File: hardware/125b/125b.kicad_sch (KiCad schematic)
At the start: 52 parts, among them J1 Guitar in, J10 Barrel_Jack, J11 NRJ6HF, J2 TC2050, J3 Conn_02x05_Odd_Even_MountingP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, SW1 Switch 1, SW2 Switch 2, SW3 RotaryEncoder_Switch, SW4 SW_DIP_x02, U1 TL074, U2 L78L05_TO92

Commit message: Start work on SMD caps and resistors
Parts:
- removed J2: TC2050, Connector_IDC:IDC-Header_2x05_P2.54mm_Vertical, symbol Connector:TC2050
- C10: renamed from C7; footprint Capacitor_THT:C_Rect_L7.0mm_W2.5mm_P5.00mm -> Capacitor_SMD:C_0805_2012Metric
- C11: renamed from C9; footprint Capacitor_THT:C_Rect_L7.0mm_W2.5mm_P5.00mm -> Capacitor_SMD:C_0805_2012Metric
- C12: renamed from C10; footprint Capacitor_THT:C_Rect_L7.0mm_W2.5mm_P5.00mm -> Capacitor_SMD:C_0805_2012Metric
- C2: renamed from C3; footprint Capacitor_THT:C_Rect_L7.0mm_W2.5mm_P5.00mm -> Capacitor_SMD:C_0805_2012Metric
- C3: renamed from C2; footprint Capacitor_THT:C_Rect_L7.0mm_W2.5mm_P5.00mm -> Capacitor_SMD:C_0805_2012Metric
- C4, C5, C6, C8: footprint Capacitor_THT:C_Rect_L7.0mm_W2.5mm_P5.00mm -> Capacitor_SMD:C_0805_2012Metric
- C7: renamed from C11; footprint Capacitor_THT:C_Rect_L7.0mm_W2.5mm_P5.00mm -> Capacitor_SMD:C_0805_2012Metric
- C9: renamed from C12; footprint Capacitor_THT:C_Rect_L7.0mm_W2.5mm_P5.00mm -> Capacitor_SMD:C_0805_2012Metric
- J3: footprint (none) -> Connector_IDC:IDC-Header_2x05_P2.54mm_Vertical
- R1: footprint Resistor_THT:R_Axial_DIN0207_L6.3mm_D2.5mm_P10.16mm_Horizontal -> Resistor_SMD:R_1206_3216Metric
- R10: renamed from R8; footprint Resistor_THT:R_Axial_DIN0207_L6.3mm_D2.5mm_P10.16mm_Horizontal -> Resistor_SMD:R_0805_2012Metric
- R11: renamed from R9; footprint Resistor_THT:R_Axial_DIN0207_L6.3mm_D2.5mm_P10.16mm_Horizontal -> Resistor_SMD:R_0805_2012Metric
- R12: renamed from R10; footprint Resistor_THT:R_Axial_DIN0207_L6.3mm_D2.5mm_P10.16mm_Horizontal -> Resistor_SMD:R_0805_2012Metric
- R13: renamed from R11; footprint Resistor_THT:R_Axial_DIN0207_L6.3mm_D2.5mm_P10.16mm_Horizontal -> Resistor_SMD:R_0805_2012Metric
- R14: renamed from R12; footprint Resistor_THT:R_Axial_DIN0207_L6.3mm_D2.5mm_P10.16mm_Horizontal -> Resistor_SMD:R_0805_2012Metric
- R15: renamed from R13; footprint Resistor_THT:R_Axial_DIN0207_L6.3mm_D2.5mm_P10.16mm_Horizontal -> Resistor_SMD:R_0805_2012Metric
- R16: renamed from R14; footprint Resistor_THT:R_Axial_DIN0207_L6.3mm_D2.5mm_P10.16mm_Horizontal -> Resistor_SMD:R_0805_2012Metric
- R17: renamed from R5; footprint Resistor_THT:R_Axial_DIN0207_L6.3mm_D2.5mm_P10.16mm_Horizontal -> Resistor_SMD:R_0805_2012Metric
- R18: renamed from R6; footprint Resistor_THT:R_Axial_DIN0207_L6.3mm_D2.5mm_P10.16mm_Horizontal -> Resistor_SMD:R_0805_2012Metric
- R19: renamed from R16; footprint Resistor_THT:R_Axial_DIN0207_L6.3mm_D2.5mm_P10.16mm_Horizontal -> Resistor_SMD:R_0805_2012Metric
- R2, R3, R4: footprint Resistor_THT:R_Axial_DIN0207_L6.3mm_D2.5mm_P10.16mm_Horizontal -> Resistor_SMD:R_0805_2012Metric
- R20: renamed from R15; footprint Resistor_THT:R_Axial_DIN0207_L6.3mm_D2.5mm_P10.16mm_Horizontal -> Resistor_SMD:R_0805_2012Metric
- R21: renamed from R17; footprint Resistor_THT:R_Axial_DIN0207_L6.3mm_D2.5mm_P10.16mm_Horizontal -> Resistor_SMD:R_0805_2012Metric
- R22: renamed from R18; footprint Resistor_THT:R_Axial_DIN0207_L6.3mm_D2.5mm_P10.16mm_Horizontal -> Resistor_SMD:R_0805_2012Metric
- R5: renamed from R19; footprint Resistor_THT:R_Axial_DIN0207_L6.3mm_D2.5mm_P10.16mm_Horizontal -> Resistor_SMD:R_0805_2012Metric
- R6: renamed from R20; footprint Resistor_THT:R_Axial_DIN0207_L6.3mm_D2.5mm_P10.16mm_Horizontal -> Resistor_SMD:R_0805_2012Metric
- R7: renamed from R21; footprint Resistor_THT:R_Axial_DIN0207_L6.3mm_D2.5mm_P10.16mm_Horizontal -> Resistor_SMD:R_0805_2012Metric
- R8: renamed from R22; footprint Resistor_THT:R_Axial_DIN0207_L6.3mm_D2.5mm_P10.16mm_Horizontal -> Resistor_SMD:R_0805_2012Metric
- R9: renamed from R7; footprint Resistor_THT:R_Axial_DIN0207_L6.3mm_D2.5mm_P10.16mm_Horizontal -> Resistor_SMD:R_0805_2012Metric
- renumbered J10 to J2, J11 to J4, SW4 to SW1, SW3 to SW2, SW1 to SW3, SW2 to SW4, U2 to U1, U1 to U2
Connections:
- net GND: now also J3.5 (Pin_5)
- net fsw7: now also J3.7 (Pin_7)
- net fsw9: now also J3.9 (Pin_9)
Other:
- moved on the sheet: J3

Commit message: Increase size of holes for switch connectors
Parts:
- SW3, SW4: footprint Connector_Wire:SolderWire-0.15sqmm_1x02_P4mm_D0.5mm_OD1.5mm -> Connector_Wire:SolderWire-0.5sqmm_1x02_P4.6mm_D0.9mm_OD2.1mm
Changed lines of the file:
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@@
 			)
 		)
-		(property "Footprint" "Connector_Wire:SolderWire-0.15sqmm_1x02_P4mm_D0.5mm_OD1.5mm"
+		(property "Footprint" "Connector_Wire:SolderWire-0.5sqmm_1x02_P4.6mm_D0.9mm_OD2.1mm"
 			(at 114.3 153.67 0)
 			(effects
@@
 			)
 		)
-		(property "Footprint" "Connector_Wire:SolderWire-0.15sqmm_1x02_P4mm_D0.5mm_OD1.5mm"
+		(property "Footprint" "Connector_Wire:SolderWire-0.5sqmm_1x02_P4.6mm_D0.9mm_OD2.1mm"
 			(at 101.6 142.24 0)
 			(effects

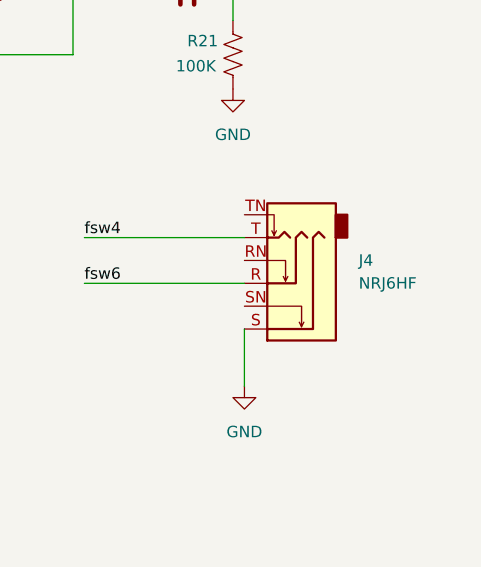
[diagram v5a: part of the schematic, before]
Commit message: Update 3d models and adjust footprints for local project lib
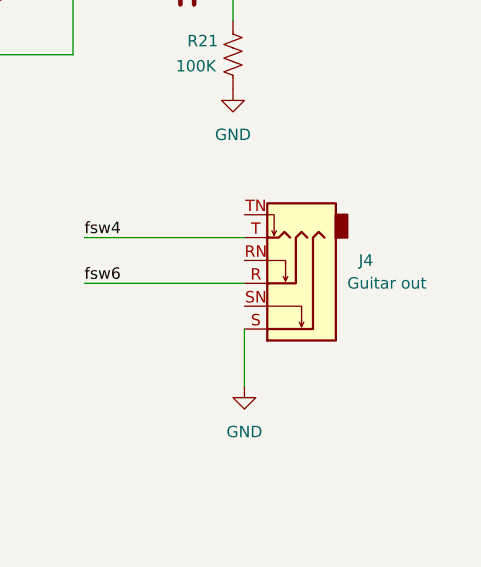
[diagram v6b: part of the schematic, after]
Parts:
- A1: footprint Module:Electrosmith_Daisy_Seed -> Library:Electrosmith_Daisy_Seed
- J1: footprint Connector_Audio:Jack_6.35mm_Neutrik_NRJ6HF-1-AU_Horizontal -> Library:Jack_6.35mm_Neutrik_NRJ6HF-1-AU_Horizontal
- J4: value NRJ6HF -> Guitar out; footprint Connector_Audio:Jack_6.35mm_Neutrik_NRJ6HF_Horizontal -> Library:Jack_6.35mm_Neutrik_NRJ6HF-1-AU_Horizontal
- RV1, RV2: footprint Potentiometer_THT:Potentiometer_Alps_RK09K_Single_Vertical -> Project:Potentiometer_Alps_RK09K_Single_Vertical
- SW2: footprint Rotary_Encoder:RotaryEncoder_Alps_EC12E-Switch_Vertical_H20mm -> Project:RotaryEncoder_Alps_EC12E-Switch_Vertical_H20mm
- U2: footprint Package_DIP:DIP-14_W7.62mm_Socket -> Package_SO:SOIC-14_3.9x8.7mm_P1.27mm
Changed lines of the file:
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@@
 			)
 		)
-		(property "Footprint" "Rotary_Encoder:RotaryEncoder_Alps_EC12E-Switch_Vertical_H20mm"
+		(property "Footprint" "Project:RotaryEncoder_Alps_EC12E-Switch_Vertical_H20mm"
 			(at 63.5 129.794 0)
 			(effects
@@
 			)
 		)
-		(property "Footprint" "Package_DIP:DIP-14_W7.62mm_Socket"
+		(property "Footprint" "Package_SO:SOIC-14_3.9x8.7mm_P1.27mm"
 			(at 139.7 41.91 0)
 			(effects
@@
 			)
 		)
-		(property "Footprint" "Package_DIP:DIP-14_W7.62mm_Socket"
+		(property "Footprint" "Package_SO:SOIC-14_3.9x8.7mm_P1.27mm"
 			(at 121.92 173.99 0)
 			(effects
@@
 			)
 		)
-		(property "Footprint" "Potentiometer_THT:Potentiometer_Alps_RK09K_Single_Vertical"
+		(property "Footprint" "Project:Potentiometer_Alps_RK09K_Single_Vertical"
 			(at 100.33 95.25 0)
 			(effects
@@
 			)
 		)
-		(property "Footprint" "Package_DIP:DIP-14_W7.62mm_Socket"
+		(property "Footprint" "Package_SO:SOIC-14_3.9x8.7mm_P1.27mm"
 			(at 231.14 30.48 0)
 			(effects
@@
 		(on_board yes)
 		(dnp no)
-		(fields_autoplaced yes)
 		(property "Reference" "J4"
 			(at 275.59 97.7899 0)
@@
 			)
 		)
-		(property "Value" "NRJ6HF"
-			(at 275.59 100.3299 0)
+		(property "Value" "Guitar out"
+			(at 274.32 100.33 0)
 			(effects
 				(font
@@
 			)
 		)
-		(property "Footprint" "Connector_Audio:Jack_6.35mm_Neutrik_NRJ6HF_Horizontal"
+		(property "Footprint" "Library:Jack_6.35mm_Neutrik_NRJ6HF-1-AU_Horizontal"
 			(at 267.97 100.33 0)
 			(effects
@@
 			)
 		)
-		(property "Footprint" "Package_DIP:DIP-14_W7.62mm_Socket"
+		(property "Footprint" "Package_SO:SOIC-14_3.9x8.7mm_P1.27mm"
 			(at 92.71 50.8 0)
 			(effects
@@
 			)
 		)
-		(property "Footprint" "Module:Electrosmith_Daisy_Seed"
+		(property "Footprint" "Library:Electrosmith_Daisy_Seed"
 			(at 181.61 140.97 0)
 			(effects
@@
 			)
 		)
-		(property "Footprint" "Package_DIP:DIP-14_W7.62mm_Socket"
+		(property "Footprint" "Package_SO:SOIC-14_3.9x8.7mm_P1.27mm"
 			(at 232.41 64.77 0)
 			(effects
@@
 			)
 		)
-		(property "Footprint" "Connector_Audio:Jack_6.35mm_Neutrik_NRJ6HF-1-AU_Horizontal"
+		(property "Footprint" "Library:Jack_6.35mm_Neutrik_NRJ6HF-1-AU_Horizontal"
 			(at 22.86 26.67 0)
 			(effects
@@
 			)
 		)
-		(property "Footprint" "Potentiometer_THT:Potentiometer_Alps_RK09K_Single_Vertical"
+		(property "Footprint" "Project:Potentiometer_Alps_RK09K_Single_Vertical"
 			(at 81.28 110.49 0)
 			(effects

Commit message: Increase RGB LED footprint for easier soldering
Also re-adjustLEDs, pots and encoder for symmetry
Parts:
- D3, D4: footprint LED_THT:LED_D5.0mm-4_RGB -> LED_THT:LED_D5.0mm-4_RGB_Wide_Pins
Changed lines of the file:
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@@
 			)
 		)
-		(property "Footprint" "LED_THT:LED_D5.0mm-4_RGB"
+		(property "Footprint" "LED_THT:LED_D5.0mm-4_RGB_Wide_Pins"
 			(at 224.79 128.27 0)
 			(effects
@@
 			)
 		)
-		(property "Footprint" "LED_THT:LED_D5.0mm-4_RGB"
+		(property "Footprint" "LED_THT:LED_D5.0mm-4_RGB_Wide_Pins"
 			(at 224.79 153.67 0)
 			(effects

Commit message: Try pin sockets for the footswitch connector
Can just solder some ribbon wire for this version
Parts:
- J3: footprint Connector_IDC:IDC-Header_2x05_P2.54mm_Vertical -> Connector_PinSocket_1.27mm:PinSocket_1x09_P1.27mm_Vertical
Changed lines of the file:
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@@
 			)
 		)
-		(property "Footprint" "Connector_IDC:IDC-Header_2x05_P2.54mm_Vertical"
+		(property "Footprint" "Connector_PinSocket_1.27mm:PinSocket_1x09_P1.27mm_Vertical"
 			(at 35.56 93.98 0)
 			(effects
